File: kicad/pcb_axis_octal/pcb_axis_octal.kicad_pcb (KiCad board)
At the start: 2 copper layers, 100 x 80 mm, 4 parts

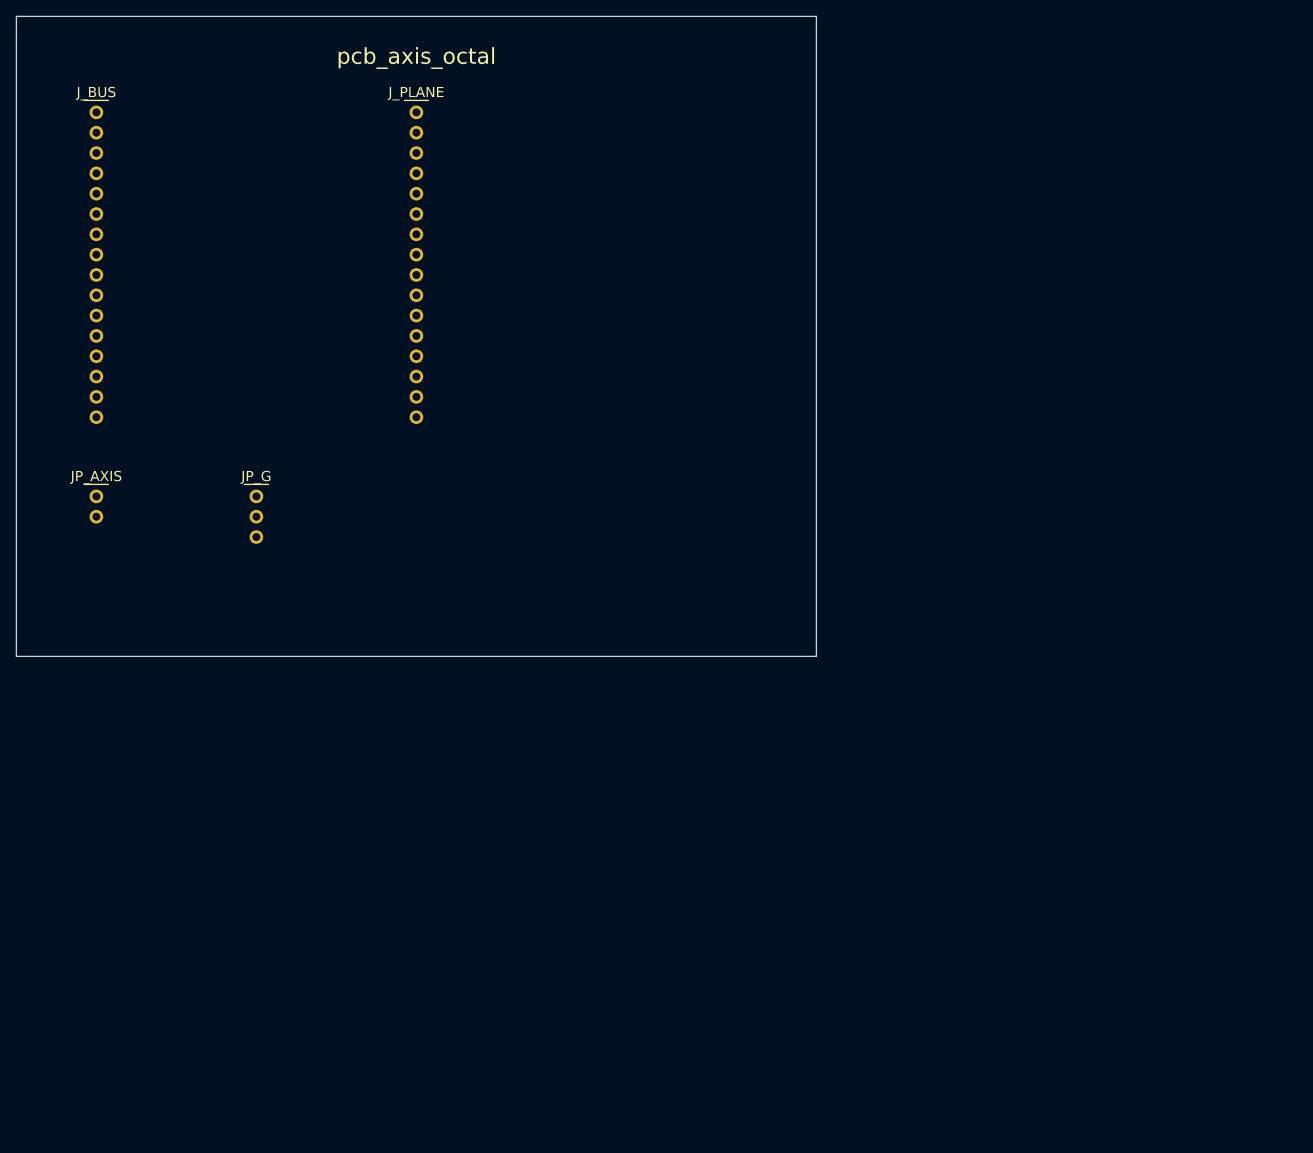
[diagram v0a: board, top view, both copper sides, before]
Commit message: logical seperation into host and multiple decode/drive/steering boards
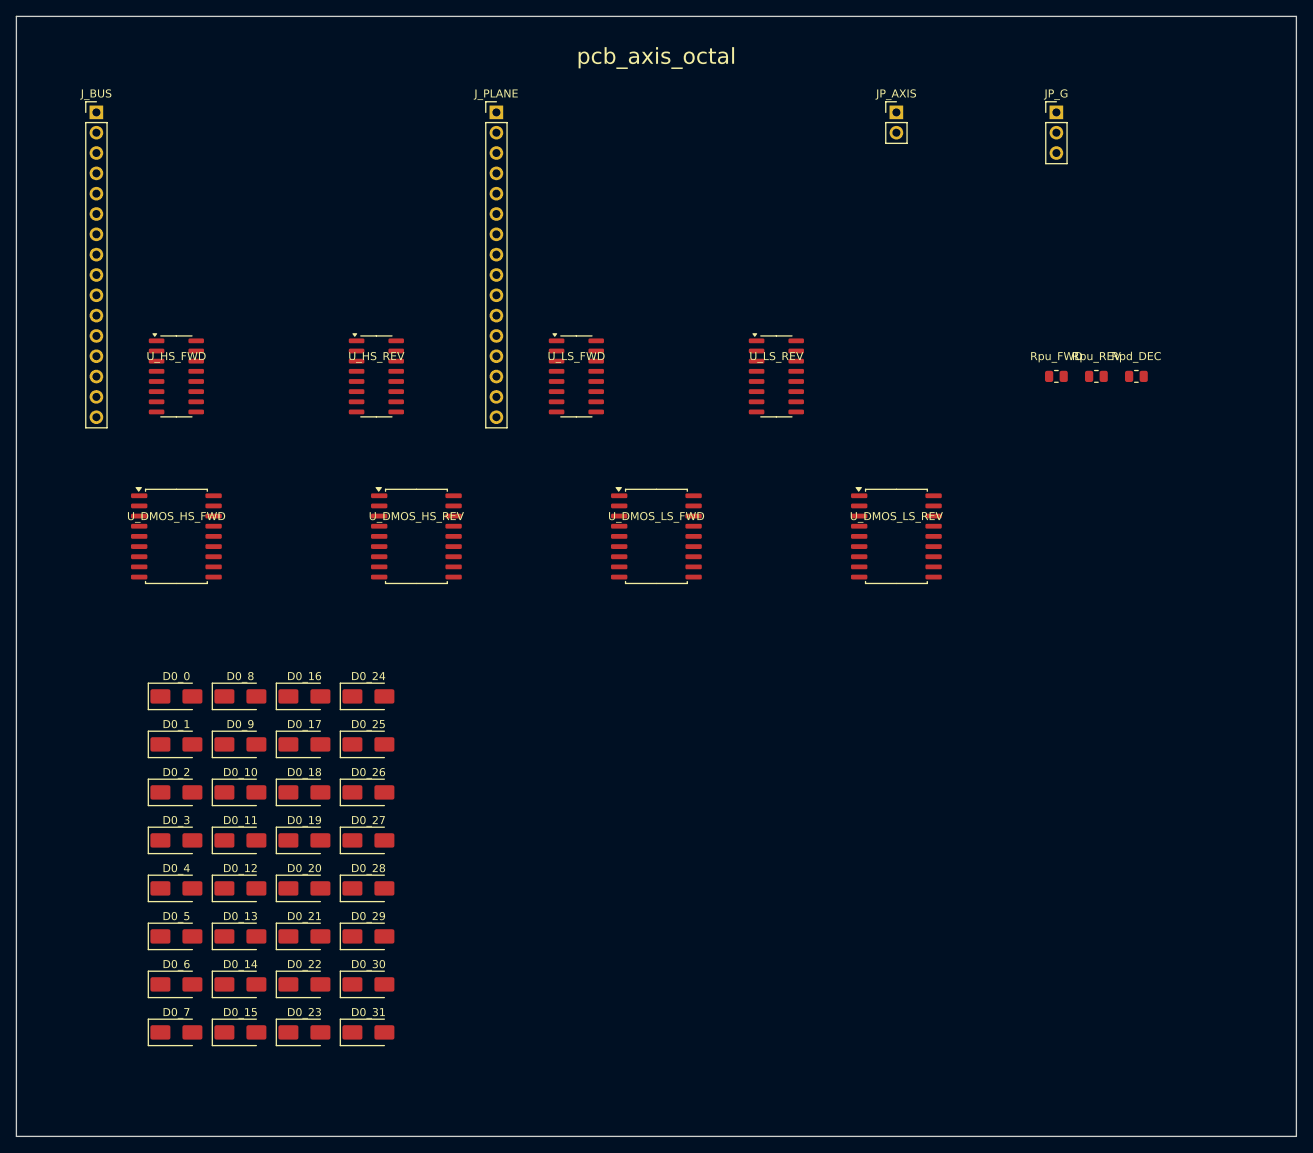
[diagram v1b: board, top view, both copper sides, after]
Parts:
- added D0_0: SS14, Diode_SMD:D_SMA, F.Cu at (20.0, 85.0)
- added D0_1: SS14, Diode_SMD:D_SMA, F.Cu at (20.0, 91.0)
- added D0_10: SS14, Diode_SMD:D_SMA, F.Cu at (28.0, 97.0)
- added D0_11: SS14, Diode_SMD:D_SMA, F.Cu at (28.0, 103.0)
- added D0_12: SS14, Diode_SMD:D_SMA, F.Cu at (28.0, 109.0)
- added D0_13: SS14, Diode_SMD:D_SMA, F.Cu at (28.0, 115.0)
- added D0_14: SS14, Diode_SMD:D_SMA, F.Cu at (28.0, 121.0)
- added D0_15: SS14, Diode_SMD:D_SMA, F.Cu at (28.0, 127.0)
- added D0_16: SS14, Diode_SMD:D_SMA, F.Cu at (36.0, 85.0)
- added D0_17: SS14, Diode_SMD:D_SMA, F.Cu at (36.0, 91.0)
- added D0_18: SS14, Diode_SMD:D_SMA, F.Cu at (36.0, 97.0)
- added D0_19: SS14, Diode_SMD:D_SMA, F.Cu at (36.0, 103.0)
- added D0_2: SS14, Diode_SMD:D_SMA, F.Cu at (20.0, 97.0)
- added D0_20: SS14, Diode_SMD:D_SMA, F.Cu at (36.0, 109.0)
- added D0_21: SS14, Diode_SMD:D_SMA, F.Cu at (36.0, 115.0)
- added D0_22: SS14, Diode_SMD:D_SMA, F.Cu at (36.0, 121.0)
- added D0_23: SS14, Diode_SMD:D_SMA, F.Cu at (36.0, 127.0)
- added D0_24: SS14, Diode_SMD:D_SMA, F.Cu at (44.0, 85.0)
- added D0_25: SS14, Diode_SMD:D_SMA, F.Cu at (44.0, 91.0)
- added D0_26: SS14, Diode_SMD:D_SMA, F.Cu at (44.0, 97.0)
- added D0_27: SS14, Diode_SMD:D_SMA, F.Cu at (44.0, 103.0)
- added D0_28: SS14, Diode_SMD:D_SMA, F.Cu at (44.0, 109.0)
- added D0_29: SS14, Diode_SMD:D_SMA, F.Cu at (44.0, 115.0)
- added D0_3: SS14, Diode_SMD:D_SMA, F.Cu at (20.0, 103.0)
- added D0_30: SS14, Diode_SMD:D_SMA, F.Cu at (44.0, 121.0)
- added D0_31: SS14, Diode_SMD:D_SMA, F.Cu at (44.0, 127.0)
- added D0_4: SS14, Diode_SMD:D_SMA, F.Cu at (20.0, 109.0)
- added D0_5: SS14, Diode_SMD:D_SMA, F.Cu at (20.0, 115.0)
- added D0_6: SS14, Diode_SMD:D_SMA, F.Cu at (20.0, 121.0)
- added D0_7: SS14, Diode_SMD:D_SMA, F.Cu at (20.0, 127.0)
- added D0_8: SS14, Diode_SMD:D_SMA, F.Cu at (28.0, 85.0)
- added D0_9: SS14, Diode_SMD:D_SMA, F.Cu at (28.0, 91.0)
- added Rpd_DEC: 10k, Resistor_SMD:R_0805_2012Metric, F.Cu at (140.0, 45.0)
- added Rpu_FWD: 10k, Resistor_SMD:R_0805_2012Metric, F.Cu at (130.0, 45.0)
- added Rpu_REV: 10k, Resistor_SMD:R_0805_2012Metric, F.Cu at (135.0, 45.0)
- added U_DMOS_HS_FWD: TBD62783, Package_SO:SOIC-18W_7.5x11.6mm_P1.27mm, F.Cu at (20.0, 65.0)
- added U_DMOS_HS_REV: TBD62783, Package_SO:SOIC-18W_7.5x11.6mm_P1.27mm, F.Cu at (50.0, 65.0)
- added U_DMOS_LS_FWD: TBD62083, Package_SO:SOIC-18W_7.5x11.6mm_P1.27mm, F.Cu at (80.0, 65.0)
- added U_DMOS_LS_REV: TBD62083, Package_SO:SOIC-18W_7.5x11.6mm_P1.27mm, F.Cu at (110.0, 65.0)
- added U_HS_FWD: 74AHC138, Package_SO:SOIC-16_3.9x9.9mm_P1.27mm, F.Cu at (20.0, 45.0)
- added U_HS_REV: 74AHC138, Package_SO:SOIC-16_3.9x9.9mm_P1.27mm, F.Cu at (45.0, 45.0)
- added U_LS_FWD: 74AHC238, Package_SO:SOIC-16_3.9x9.9mm_P1.27mm, F.Cu at (70.0, 45.0)
- added U_LS_REV: 74AHC238, Package_SO:SOIC-16_3.9x9.9mm_P1.27mm, F.Cu at (95.0, 45.0)
- JP_AXIS: footprint Connector_PinHeader_2.54mm:PinHeader_1x2_P2.54mm_Vertical -> Connector_PinHeader_2.54mm:PinHeader_1x02_P2.54mm_Vertical
- JP_G: footprint Connector_PinHeader_2.54mm:PinHeader_1x3_P2.54mm_Vertical -> Connector_PinHeader_2.54mm:PinHeader_1x03_P2.54mm_Vertical
- moved JP_AXIS 110.9 mm to (110.0, 12.0)
- moved JP_G 110.9 mm to (130.0, 12.0)
- moved J_PLANE 10.0 mm to (60.0, 12.0)
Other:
- board size 100 x 80 mm -> 160 x 140 mm
